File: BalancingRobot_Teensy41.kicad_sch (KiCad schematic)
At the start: 0 parts

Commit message: Completed Schematic and the DRC also passes
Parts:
- added C1, C3: 100n, Capacitor_THT:C_Disc_D5.0mm_W2.5mm_P5.00mm, symbol Device:C
- added C2, C4, C5, C6: 10n, Capacitor_THT:C_Disc_D5.0mm_W2.5mm_P5.00mm, symbol Device:C
- added J1, J4, J5: Conn_01x06_Socket, Connector_JST:JST_PH_S6B-PH-K_1x06_P2.00mm_Horizontal, symbol Connector:Conn_01x06_Socket
- added J2: Conn_01x04_Socket, Connector_JST:JST_PH_S4B-PH-K_1x04_P2.00mm_Horizontal, symbol Connector:Conn_01x04_Socket
- added J3: Conn_01x02_Socket, Connector_AMASS:AMASS_XT30U-F_1x02_P5.0mm_Vertical, symbol Connector:Conn_01x02_Socket
- added R1, R3: 10k, Resistor_THT:R_Axial_DIN0204_L3.6mm_D1.6mm_P7.62mm_Horizontal, symbol Device:R_US
- added R2, R4: 1k, Resistor_THT:R_Axial_DIN0204_L3.6mm_D1.6mm_P7.62mm_Horizontal, symbol Device:R_US
- added U1: Teensy4.1, Teensy41:Teensy41, symbol Teensy:Teensy4.1
- added U2: ICM20948_Carrier_Board, Adafruit_ICM20948:ICM20948_Carrier, symbol ICM20948_Carrier:ICM20948_Carrier
- added U3, U4: DRV8874_Carrier, Pololu_DRV8874:DRV8874_Carrier, symbol DRV8874_Carrier:DRV8874_Carrier
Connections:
- new net: C4.1, J5.1 (Pin_1), U4.11 (OUT2)
- new net: C3.1, J5.6 (Pin_6), U4.12 (OUT1)
- new net: R4.1, U4.8 (CS)
- new net: C2.1, J4.1 (Pin_1), U3.11 (OUT2)
- new net: C1.1, J4.6 (Pin_6), U3.12 (OUT1)
- new net: R2.1, U3.8 (CS)
- new net +12V: J3.1 (Pin_1), U3.14 (VIN), U4.14 (VIN)
- new net +3V3: J2.1 (Pin_1), J4.2 (Pin_2), J5.2 (Pin_2), R1.1, R3.1, U1.46 (3V3), U2.1 (VIN)
- new net +5V: J1.1 (Pin_1), J1.2 (Pin_2), U1.48 (VIN)
- new net ENC_A_PH_A: J4.3 (Pin_3), U1.2 (0_ENC_A_PH_A)
- new net ENC_A_PH_B: J4.4 (Pin_4), U1.3 (1_ENC_A_PH_B)
- new net ENC_B_PH_A: J5.3 (Pin_3), U1.23 (31_ENC_B_PH_A)
- new net ENC_B_PH_B: J5.4 (Pin_4), U1.24 (32_ENC_B_PH_B)
- new net GND: C1.2, C2.2, C3.2, C4.2, C5.2, C6.2, J1.5 (Pin_5), J1.6 (Pin_6), J2.4 (Pin_4), J3.2 (Pin_2), J4.5 (Pin_5), J5.5 (Pin_5), U1.1 (GND), U1.34 (GND), U1.47 (GND), U2.3 (GND), U2.9 (GND), U3.13 (GND), U3.2 (GND), U3.5 (PMODE), U4.13 (GND), U4.2 (GND), U4.5 (PMODE)
- new net ICM20948_CS: U1.12 (10_SPI0_CS), U2.7 (CS)
- new net ICM20948_INT: U1.39 (17_ICM20948_INT), U2.6 (INT)
- new net ICM20948_SCL: U1.35 (13_SPI0_SCK), U2.4 (SCK/SCL)
- new net ICM20948_SDI: U1.13 (11_SPI0_MOSI), U2.5 (SDI/SDA)
- new net ICM20948_SDO: U1.14 (12_SPI0_MISO), U2.8 (SDO/ADR)
- new net MOTA_CUR: C5.1, R2.2, U1.42 (20_MOTA_CUR)
- new net MOTA_DIR: U1.5 (3_MOTA_DIR), U3.4 (PH/IN2)
- new net MOTA_FAULT: R1.2, U1.25 (33_MOTA_FAULT), U3.9 (FAULT)
- new net MOTA_PWM: U1.4 (2_MOTA_PWM), U3.3 (EN/IN1)
- new net MOTA_SLEEP: U1.21 (29_MOTA_SLEEP), U3.6 (SLEEP)
- new net MOTB_CUR: C6.1, R4.2, U1.43 (21_MOTB_CUR)
- new net MOTB_DIR: U1.8 (6_MOTB_DIR), U4.4 (PH/IN2)
- new net MOTB_FAULT: R3.2, U1.26 (34_MOTB_FAULT), U4.9 (FAULT)
- new net MOTB_PWM: U1.7 (5_MOTB_PWM), U4.3 (EN/IN1)
- new net MOTB_SLEEP: U1.22 (30_MOTB_SLEEP), U4.6 (SLEEP)
- new net PM02_SCL: J1.3 (Pin_3), U1.41 (19_PM02_SCL)
- new net PM02_SDA: J1.4 (Pin_4), U1.40 (18_PM02_SDA)
- new net UART_COMP_RX: J2.2 (Pin_2), U1.9 (7_COMP_RX)
- new net UART_COMP_TX: J2.3 (Pin_3), U1.10 (8_COMP_TX)
- no-connect marks 0 -> 49
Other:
- note added: "ICM20948 Carrier Board"
- note added: "Motor - A"
- note added: "Motor - B"
- note added: "Motor Power"
- note added: "Power from Power Module - PM02D"
- note added: "UART Companion Computer"

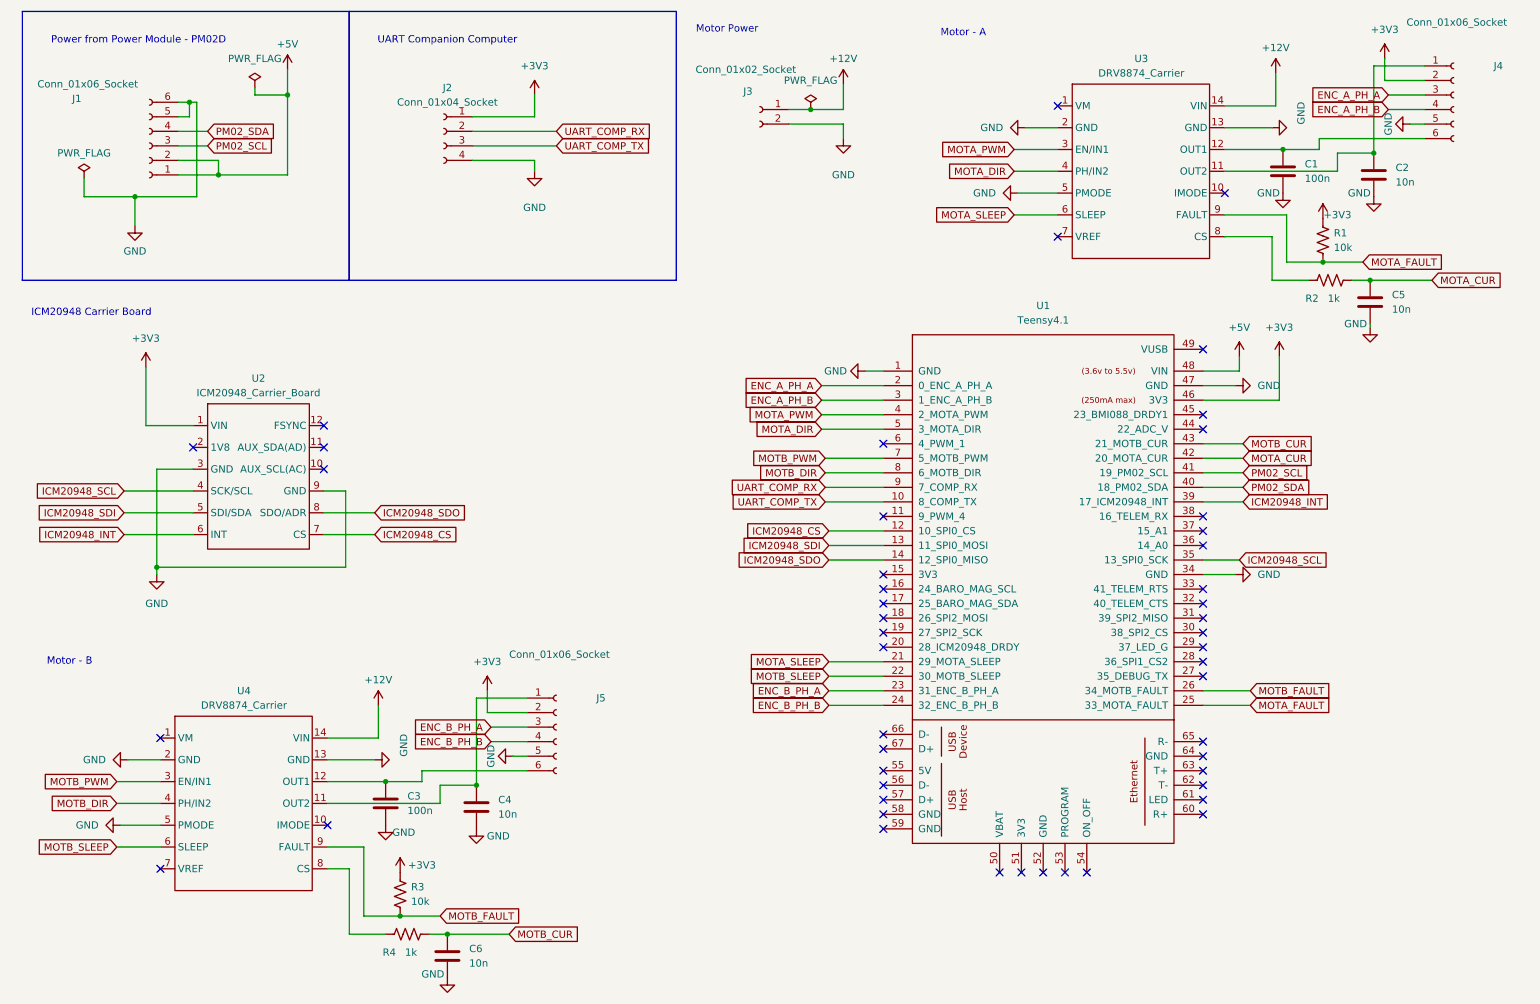
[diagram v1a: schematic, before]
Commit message: Added bulk caps for VIN on Teensy and Motor Controllers
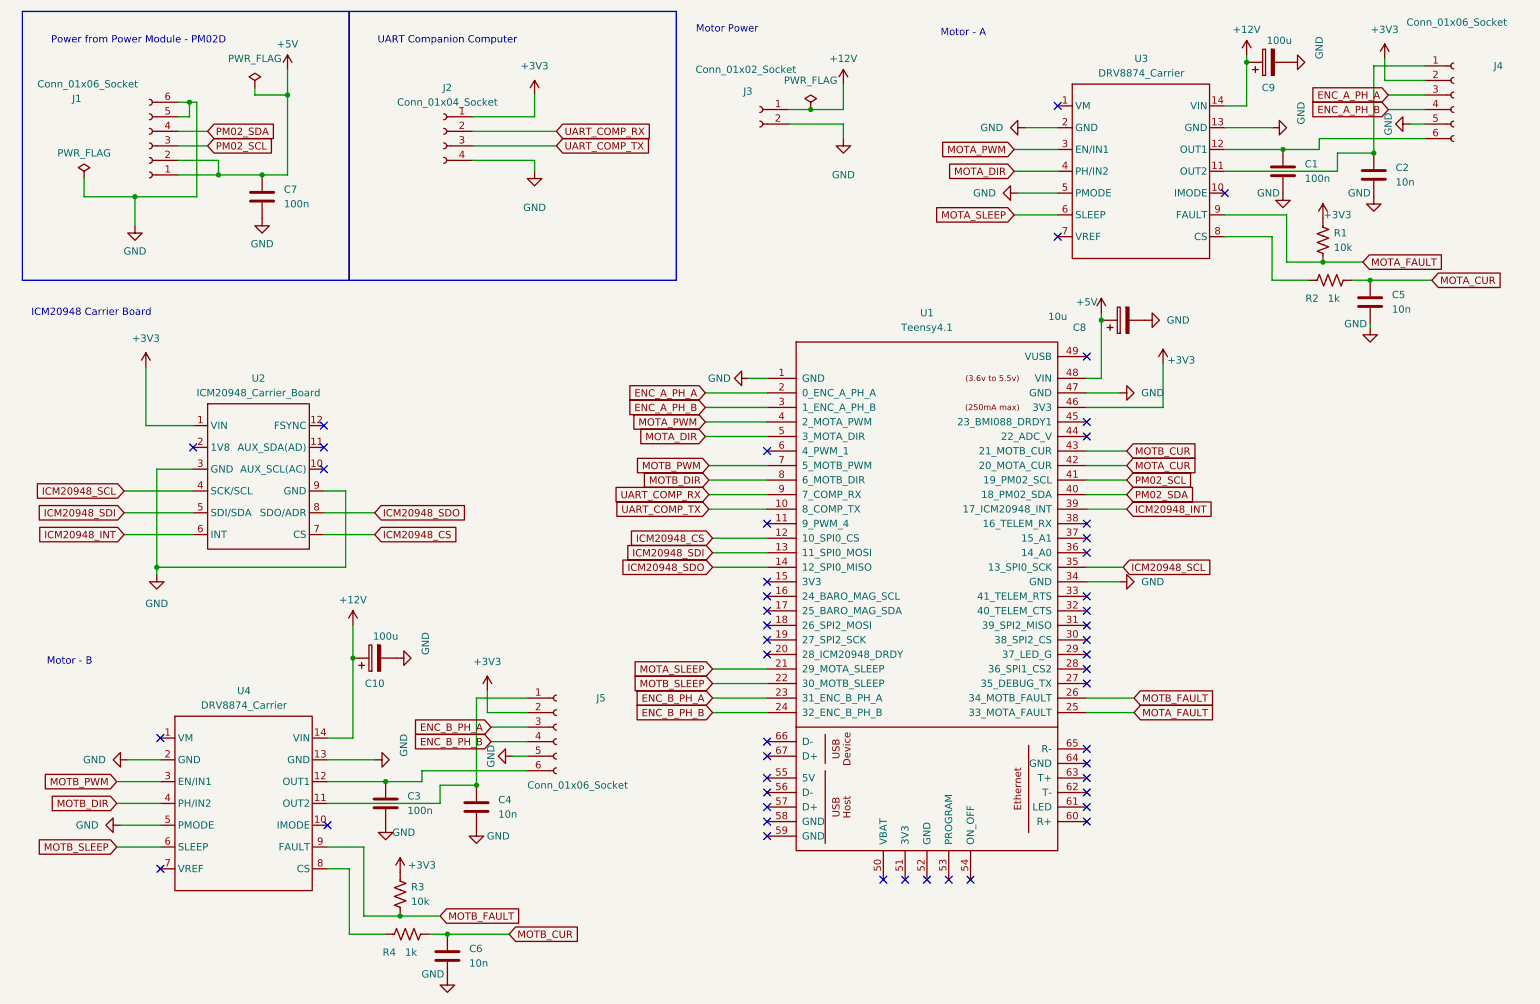
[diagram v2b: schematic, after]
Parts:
- added C10, C9: 100u, Capacitor_THT:CP_Radial_D5.0mm_P2.50mm, symbol Device:C_Polarized
- added C7: 100n, Capacitor_THT:C_Disc_D5.0mm_W2.5mm_P5.00mm, symbol Device:C
- added C8: 10u, Capacitor_THT:CP_Radial_D5.0mm_P2.50mm, symbol Device:C_Polarized
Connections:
- net +12V: now also C10.1, C9.1
- net +5V: now also C7.1, C8.1
- net GND: now also C10.2, C7.2, C8.2, C9.2
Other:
- moved on the sheet: U1

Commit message: Split busy schematic into subpages. Mainly moved ICM20948 and the two motor controllers to inidividual pages
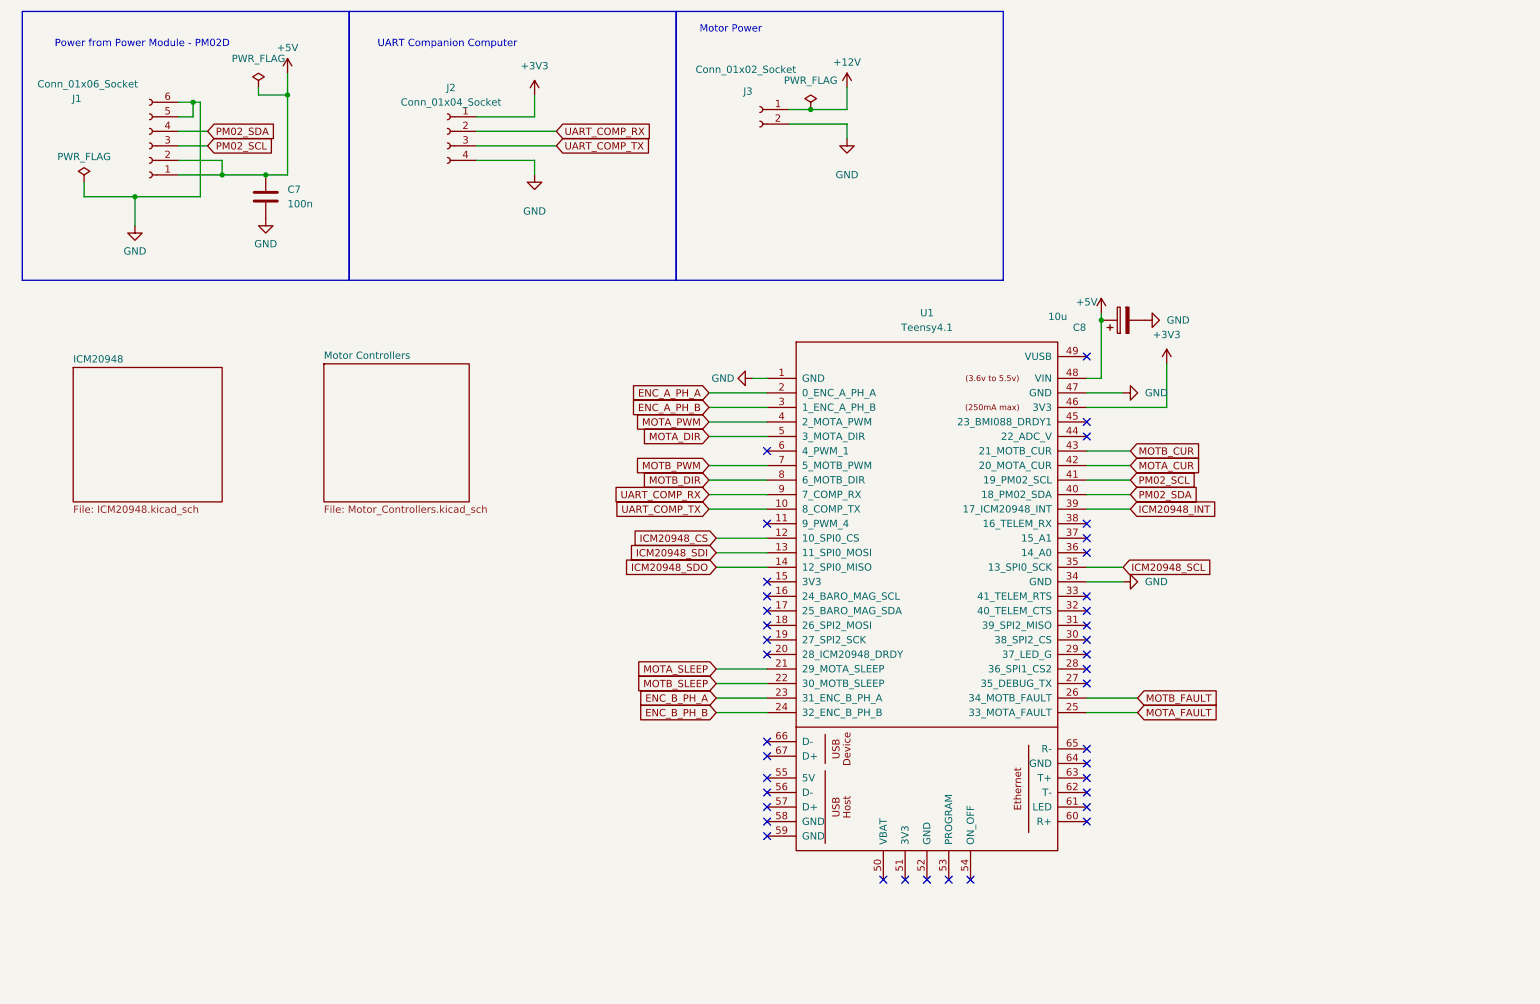
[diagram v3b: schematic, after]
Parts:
- removed C1, C3: 100n, Capacitor_THT:C_Disc_D5.0mm_W2.5mm_P5.00mm, symbol Device:C
- removed C10, C9: 100u, Capacitor_THT:CP_Radial_D5.0mm_P2.50mm, symbol Device:C_Polarized
- removed C2, C4, C5, C6: 10n, Capacitor_THT:C_Disc_D5.0mm_W2.5mm_P5.00mm, symbol Device:C
- removed J4, J5: Conn_01x06_Socket, Connector_JST:JST_PH_S6B-PH-K_1x06_P2.00mm_Horizontal, symbol Connector:Conn_01x06_Socket
- removed R1, R3: 10k, Resistor_THT:R_Axial_DIN0204_L3.6mm_D1.6mm_P7.62mm_Horizontal, symbol Device:R_US
- removed R2, R4: 1k, Resistor_THT:R_Axial_DIN0204_L3.6mm_D1.6mm_P7.62mm_Horizontal, symbol Device:R_US
- removed U2: ICM20948_Carrier_Board, Adafruit_ICM20948:ICM20948_Carrier, symbol ICM20948_Carrier:ICM20948_Carrier
- removed U3, U4: DRV8874_Carrier, Pololu_DRV8874:DRV8874_Carrier, symbol DRV8874_Carrier:DRV8874_Carrier
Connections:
- no-connect marks 49 -> 39
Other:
- added sheet ICM20948 (ICM20948.kicad_sch)
- added sheet Motor Controllers (Motor_Controllers.kicad_sch)
- note removed: "ICM20948 Carrier Board"
- note removed: "Motor - A"
- note removed: "Motor - B"
- moved on the sheet: C7, J2

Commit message: Started with routing
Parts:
- J1: value Conn_01x06_Socket -> PM02D
- J2: value Conn_01x04_Socket -> UART
- J3: value Conn_01x02_Socket -> XT30
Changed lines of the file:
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@@
 			)
 		)
-		(property "Value" "Conn_01x02_Socket"
+		(property "Value" "XT30"
 			(at 147.32 22.225 0)
 			(effects
@@
 			)
 		)
-		(property "Value" "Conn_01x06_Socket"
+		(property "Value" "PM02D"
 			(at 23.495 24.765 0)
 			(effects
@@
 			)
 		)
-		(property "Value" "Conn_01x04_Socket"
+		(property "Value" "UART"
 			(at 86.995 27.94 0)
 			(effects
